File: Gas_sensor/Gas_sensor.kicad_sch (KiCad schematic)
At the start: 144 parts, among them J1 Conn_02x02_Counter_Clockwise, J2 Conn_01x04, J3 Conn_01x10, J4 Conn_01x01, J5 Conn_01x01, Q1 DMC1229UFDB, Q2 DMC1229UFDB, Q3 Q_NMOS_GSD, Q4 Q_NMOS_GSD, Q5 Q_NMOS_GSD, Q6 Q_NMOS_GSD, SW1 SW_Push, SW10 SW_Push, SW11 SW_Push, SW12 SW_Push, SW2 SW_Push, SW3 SW_Push, SW4 SW_Push, SW5 SW_Push, SW6 SW_Push, SW7 SW_Push, SW8 SW_Push, SW9 SW_Push, U1 LPV511, U10 MCP1700-3302E_SOT23, U11 STM32F401CCUx, U12 TMP117, U13 TPS63070, U14 TPS79333-EP, U15 REG102GA, U2 LPV511, U3 MCP47CMB22, U4 MCP6V71, U5 LPV511, U6 MCP6V71, U7 MCP6V71, U8 MCP6V71, U9 ADS1115IDGS, Y1 25MHz

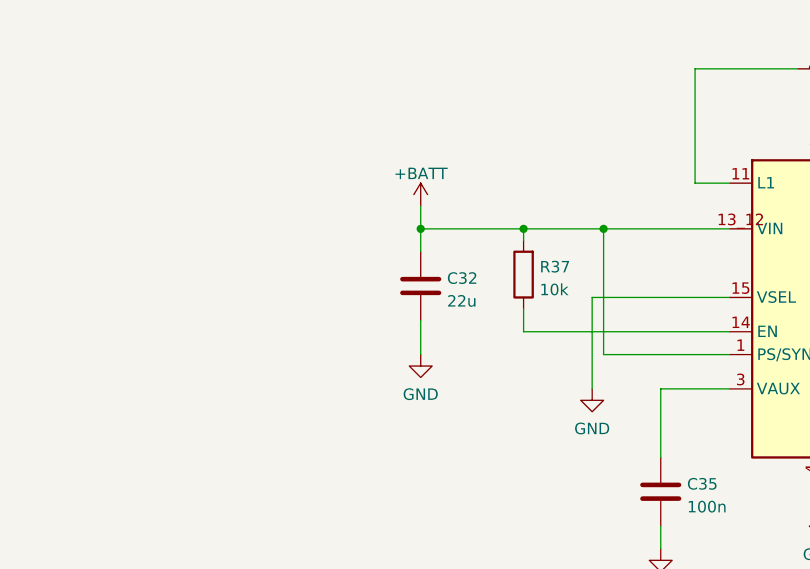
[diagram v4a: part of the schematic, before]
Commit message: gas sensor : place components
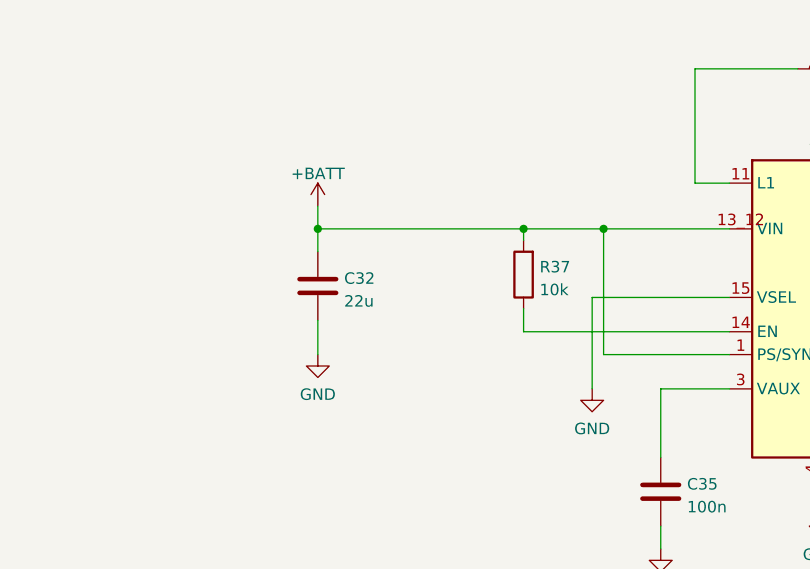
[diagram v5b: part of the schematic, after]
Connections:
- net at U3.5 (Vout1): now also R7.1
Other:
- moved on the sheet: C32
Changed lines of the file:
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@@
   (junction (at 237.49 318.77) (diameter 0) (color 0 0 0 0)
   )
-  (junction (at 466.09 82.55) (diameter 0) (color 0 0 0 0)
+  (junction (at 454.66 82.55) (diameter 0) (color 0 0 0 0)
   )
   (junction (at 497.84 279.4) (diameter 0) (color 0 0 0 0)
@@
     (stroke (width 0) (type default) (color 0 0 0 0))
   )
-  (wire (pts (xy 466.09 82.55) (xy 466.09 85.09))
+  (wire (pts (xy 454.66 82.55) (xy 454.66 85.09))
     (stroke (width 0) (type default) (color 0 0 0 0))
   )
@@
     (stroke (width 0) (type default) (color 0 0 0 0))
   )
-  (wire (pts (xy 477.52 82.55) (xy 466.09 82.55))
+  (wire (pts (xy 477.52 82.55) (xy 454.66 82.55))
     (stroke (width 0) (type default) (color 0 0 0 0))
   )
@@
     (stroke (width 0) (type default) (color 0 0 0 0))
   )
-  (wire (pts (xy 466.09 80.01) (xy 466.09 82.55))
+  (wire (pts (xy 454.66 80.01) (xy 454.66 82.55))
     (stroke (width 0) (type default) (color 0 0 0 0))
   )
@@
     (stroke (width 0) (type default) (color 0 0 0 0))
   )
-  (wire (pts (xy 466.09 92.71) (xy 466.09 96.52))
+  (wire (pts (xy 454.66 92.71) (xy 454.66 96.52))
     (stroke (width 0) (type default) (color 0 0 0 0))
   )
@@
     (pin "1")
   )
-  (symbol (lib_id "Device:C") (at 466.09 88.9 0) (unit 1)
+  (symbol (lib_id "Device:C") (at 454.66 88.9 0) (unit 1)
     (in_bom yes) (on_board yes) (fields_autoplaced)
-    (property "Reference" "C32" (id 0) (at 469.011 88.0653 0)
+    (property "Reference" "C32" (id 0) (at 457.581 88.0653 0)
       (effects (font (size 1.27 1.27)) (justify left))
     )
-    (property "Value" "22u" (id 1) (at 469.011 90.6022 0)
+    (property "Value" "22u" (id 1) (at 457.581 90.6022 0)
       (effects (font (size 1.27 1.27)) (justify left))
     )
-    (property "Footprint" "Yame_library:SM0603-MR" (id 2) (at 467.0552 92.71 0)
+    (property "Footprint" "Yame_library:SM0603-MR" (id 2) (at 455.6252 92.71 0)
       (effects (font (size 1.27 1.27)) hide)
     )
-    (property "Datasheet" "~" (id 3) (at 466.09 88.9 0)
+    (property "Datasheet" "~" (id 3) (at 454.66 88.9 0)
       (effects (font (size 1.27 1.27)) hide)
     )
@@
     (pin "2")
   )
-  (symbol (lib_id "power:+BATT") (at 466.09 80.01 0) (unit 1)
+  (symbol (lib_id "power:+BATT") (at 454.66 80.01 0) (unit 1)
     (in_bom yes) (on_board yes) (fields_autoplaced)
-    (property "Reference" "#PWR0104" (id 0) (at 466.09 83.82 0)
+    (property "Reference" "#PWR0104" (id 0) (at 454.66 83.82 0)
       (effects (font (size 1.27 1.27)) hide)
     )
-    (property "Value" "+BATT" (id 1) (at 466.09 76.4342 0))
-    (property "Footprint" "" (id 2) (at 466.09 80.01 0)
+    (property "Value" "+BATT" (id 1) (at 454.66 76.4342 0))
+    (property "Footprint" "" (id 2) (at 454.66 80.01 0)
       (effects (font (size 1.27 1.27)) hide)
     )
-    (property "Datasheet" "" (id 3) (at 466.09 80.01 0)
+    (property "Datasheet" "" (id 3) (at 454.66 80.01 0)
       (effects (font (size 1.27 1.27)) hide)
     )
@@
     (pin "2")
   )
-  (symbol (lib_id "power:GND") (at 466.09 96.52 0) (unit 1)
+  (symbol (lib_id "power:GND") (at 454.66 96.52 0) (unit 1)
     (in_bom yes) (on_board yes) (fields_autoplaced)
-    (property "Reference" "#PWR0105" (id 0) (at 466.09 102.87 0)
+    (property "Reference" "#PWR0105" (id 0) (at 454.66 102.87 0)
       (effects (font (size 1.27 1.27)) hide)
     )
-    (property "Value" "GND" (id 1) (at 466.09 100.9634 0))
-    (property "Footprint" "" (id 2) (at 466.09 96.52 0)
+    (property "Value" "GND" (id 1) (at 454.66 100.9634 0))
+    (property "Footprint" "" (id 2) (at 454.66 96.52 0)
       (effects (font (size 1.27 1.27)) hide)
     )
-    (property "Datasheet" "" (id 3) (at 466.09 96.52 0)
+    (property "Datasheet" "" (id 3) (at 454.66 96.52 0)
       (effects (font (size 1.27 1.27)) hide)
     )

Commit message: update layout
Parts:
- removed C27: 100n, Yame_library:SM0201-MR, symbol Device:C
- removed D1: BAT54C, Package_TO_SOT_SMD:SOT-23, symbol Diode:BAT54C
- added C46: 10u, Yame_library:SM0603-MR, symbol Device:C
- C16, C17, C18: footprint Yame_library:SM0603-MR -> Yame_library:SM0402-MR
- R1, R17, R19, R2, R24: footprint Yame_library:SM0402-MR -> Yame_library:SM0201-MR
- Y1: footprint Oscillator:Oscillator_SMD_Abracon_ASE-4Pin_3.2x2.5mm_HandSoldering -> Crystal:Crystal_SMD_3225-4Pin_3.2x2.5mm
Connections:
- net +3V3: now also C26.1, U11.1 (VBAT)
- net +BATT: now also C46.1
- net APO: now also U11.39 (PB3); no longer U11.46 (PB9)
- net GND: now also J1.2 (Pin_2), J1.3 (Pin_3), C46.2; no longer J1.1 (Pin_1), J1.4 (Pin_4)
- net ~{RDY}: now also U11.20 (PB2)
- net at U3.5 (Vout1): now also R7.1
- net at Q1.3 (D2), Q1.8 (D2), U7.3 (+): now also J1.1 (Pin_1); no longer J1.2 (Pin_2)
- net at Q2.3 (D2), Q2.8 (D2), U8.3 (+): now also J1.4 (Pin_4); no longer J1.3 (Pin_3)
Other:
- moved on the sheet: J1

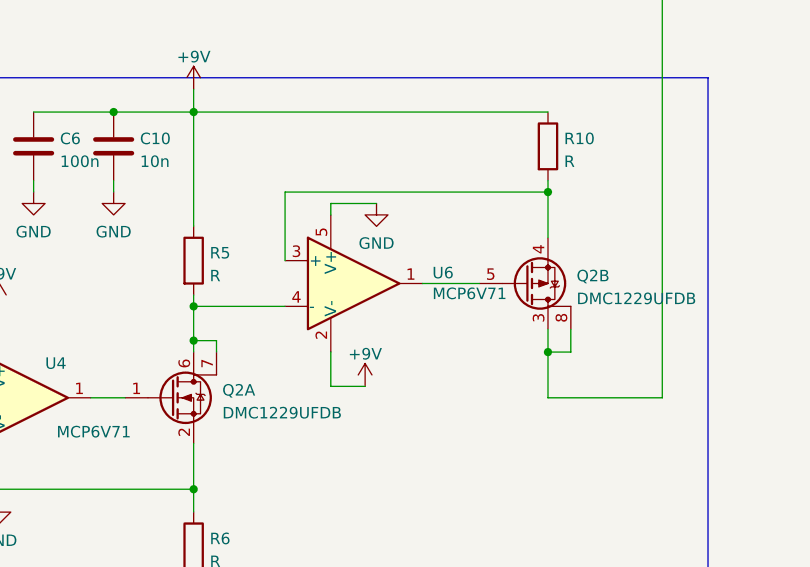
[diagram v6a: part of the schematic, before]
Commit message: Gas sensor : update layout
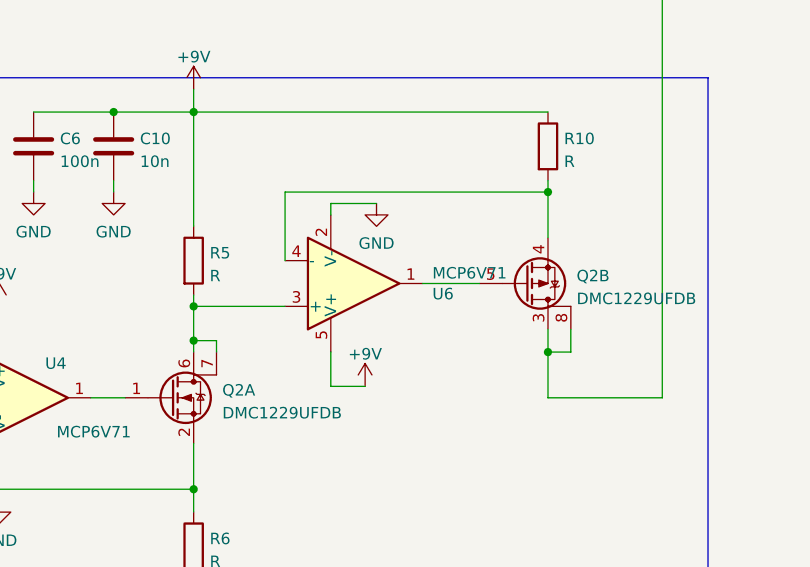
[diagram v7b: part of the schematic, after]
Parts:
- U1, U2: footprint Package_TO_SOT_SMD:SOT-23-5 -> Package_TO_SOT_SMD:SOT-353_SC-70-5
- U4: footprint Package_TO_SOT_SMD:SOT-353_SC-70-5 -> Package_TO_SOT_SMD:SOT-23-5
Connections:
- net +9V: now also U6.5 (V+); no longer U6.2 (V-)
- net GND: now also U6.2 (V-); no longer U6.5 (V+)
- net at Q2.4 (S2), R10.2: now also U6.4 (-); no longer U6.3 (+)
- net at Q2.6 (D1), Q2.7 (D1), R5.2: now also U6.3 (+); no longer U6.4 (-)
- net at U3.5 (Vout1): now also R7.1
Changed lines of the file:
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@@
       (effects (font (size 1.27 1.27)) (justify left))
     )
-    (property "Footprint" "Package_TO_SOT_SMD:SOT-23-5" (id 2) (at 110.49 87.63 0)
+    (property "Footprint" "Package_TO_SOT_SMD:SOT-353_SC-70-5" (id 2) (at 110.49 87.63 0)
       (effects (font (size 1.27 1.27)) (justify left) hide)
     )
@@
     (pin "2")
   )
-  (symbol (lib_id "Amplifier_Operational:LPV811DBV") (at 166.37 207.01 0) (unit 1)
+  (symbol (lib_id "Amplifier_Operational:LPV811DBV") (at 166.37 207.01 0) (mirror x) (unit 1)
     (in_bom yes) (on_board yes)
-    (property "Reference" "U6" (id 0) (at 175.1076 205.8416 0)
+    (property "Reference" "U6" (id 0) (at 175.1076 208.1784 0)
       (effects (font (size 1.27 1.27)) (justify left))
     )
-    (property "Value" "MCP6V71" (id 1) (at 175.1076 208.153 0)
+    (property "Value" "MCP6V71" (id 1) (at 175.1076 205.867 0)
       (effects (font (size 1.27 1.27)) (justify left))
     )
-    (property "Footprint" "Package_TO_SOT_SMD:SOT-23-5" (id 2) (at 163.83 212.09 0)
+    (property "Footprint" "Package_TO_SOT_SMD:SOT-23-5" (id 2) (at 163.83 201.93 0)
       (effects (font (size 1.27 1.27)) (justify left) hide)
     )
-    (property "Datasheet" "https://www.ti.com/lit/ds/symlink/lpv812.pdf" (id 3) (at 166.37 201.93 0)
+    (property "Datasheet" "https://www.ti.com/lit/ds/symlink/lpv812.pdf" (id 3) (at 166.37 212.09 0)
       (effects (font (size 1.27 1.27)) hide)
     )
@@
       (effects (font (size 1.27 1.27)) (justify left))
     )
-    (property "Footprint" "Package_TO_SOT_SMD:SOT-353_SC-70-5" (id 2) (at 127 224.79 0)
+    (property "Footprint" "Package_TO_SOT_SMD:SOT-23-5" (id 2) (at 127 224.79 0)
       (effects (font (size 1.27 1.27)) (justify left) hide)
     )
@@
       (effects (font (size 1.27 1.27)) (justify left))
     )
-    (property "Footprint" "Package_TO_SOT_SMD:SOT-23-5" (id 2) (at 68.58 354.33 0)
+    (property "Footprint" "Package_TO_SOT_SMD:SOT-353_SC-70-5" (id 2) (at 68.58 354.33 0)
       (effects (font (size 1.27 1.27)) (justify left) hide)
     )
@@
     )
     (path "/c639d856-1978-4de2-9271-4ecaf053f77d"
-      (reference "U1") (unit 1) (value "LPV511") (footprint "Package_TO_SOT_SMD:SOT-23-5")
+      (reference "U1") (unit 1) (value "LPV511") (footprint "Package_TO_SOT_SMD:SOT-353_SC-70-5")
     )
     (path "/00000000-0000-0000-0000-000062f6e0e7"
-      (reference "U2") (unit 1) (value "LPV511") (footprint "Package_TO_SOT_SMD:SOT-23-5")
+      (reference "U2") (unit 1) (value "LPV511") (footprint "Package_TO_SOT_SMD:SOT-353_SC-70-5")
     )
     (path "/3bc90c99-6b90-4d5e-a510-a209a2e89490"
@@
     )
     (path "/a6f7638d-f863-4fef-b4b7-b44c93155bb9"
-      (reference "U4") (unit 1) (value "MCP6V71") (footprint "Package_TO_SOT_SMD:SOT-353_SC-70-5")
+      (reference "U4") (unit 1) (value "MCP6V71") (footprint "Package_TO_SOT_SMD:SOT-23-5")
     )
     (path "/ea765fe7-c21d-4dd9-96b4-f61518ce7189"

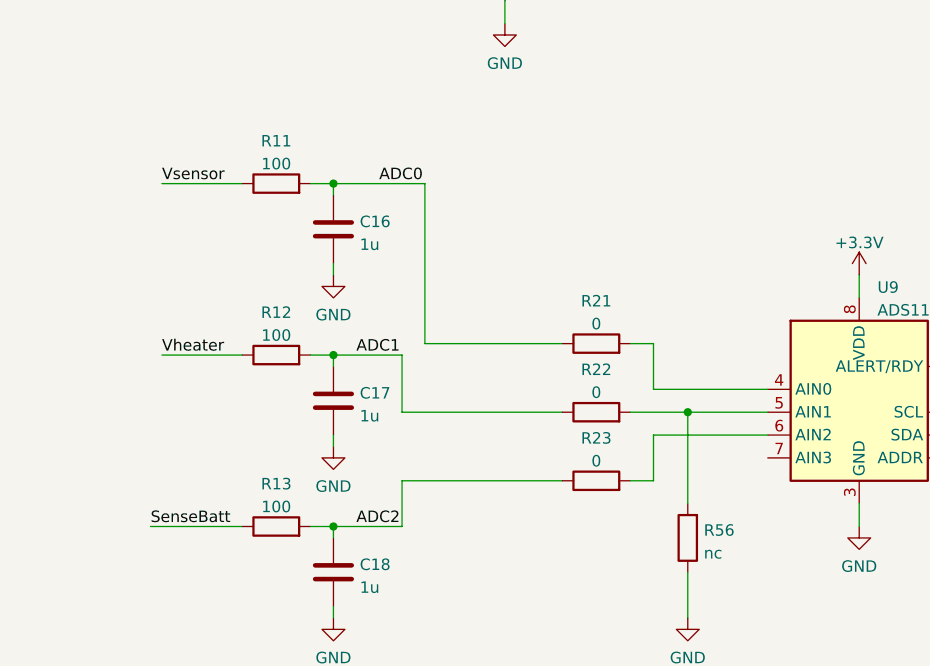
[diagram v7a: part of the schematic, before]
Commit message: gas sensor : update layout
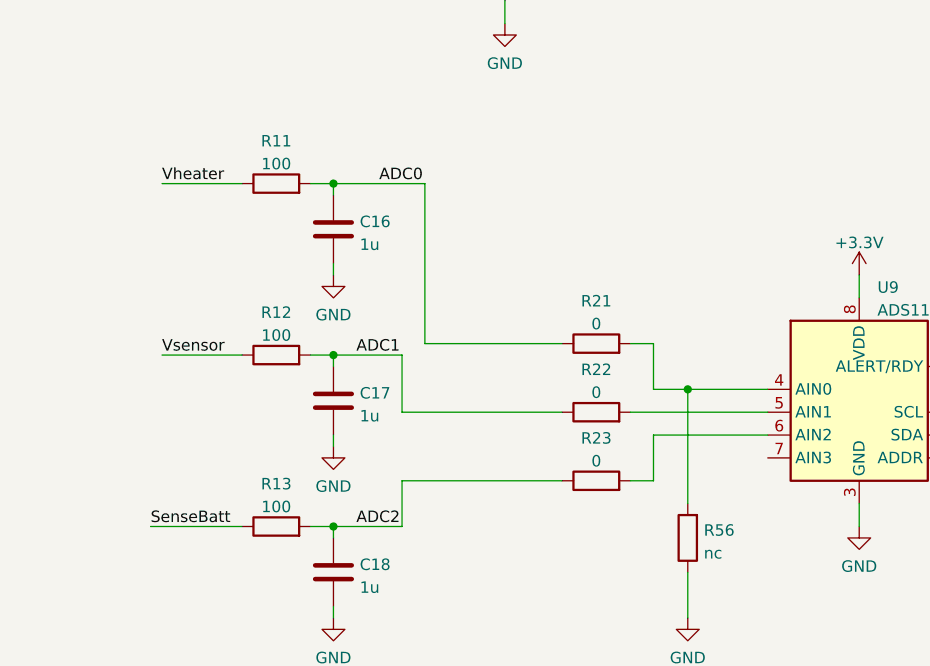
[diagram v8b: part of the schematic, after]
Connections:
- net Vheater: now also R11.1; no longer R12.1
- net Vsensor: now also R12.1; no longer R11.1
- net at R22.2, U9.5 (AIN1): no longer R56.2
- net at U3.5 (Vout1): now also R7.1
- net at R21.2, U9.4 (AIN0): now also R56.2
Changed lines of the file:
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@@
   (junction (at 237.49 356.87) (diameter 0) (color 0 0 0 0)
   )
+  (junction (at 276.86 341.63) (diameter 0) (color 0 0 0 0)
+  )
   (junction (at 312.42 114.3) (diameter 0) (color 0 0 0 0)
   )
@@
   (junction (at 438.15 152.4) (diameter 0) (color 0 0 0 0)
   )
-  (junction (at 276.86 344.17) (diameter 0) (color 0 0 0 0)
-  )
   (junction (at 132.08 76.2) (diameter 0) (color 0 0 0 0)
   )
@@
     (stroke (width 0) (type default) (color 0 0 0 0))
   )
-  (wire (pts (xy 273.05 341.63) (xy 285.75 341.63))
+  (wire (pts (xy 273.05 341.63) (xy 276.86 341.63))
     (stroke (width 0) (type default) (color 0 0 0 0))
   )
@@
     (stroke (width 0) (type default) (color 0 0 0 0))
   )
+  (wire (pts (xy 276.86 341.63) (xy 285.75 341.63))
+    (stroke (width 0) (type default) (color 0 0 0 0))
+  )
   (wire (pts (xy 542.29 106.68) (xy 542.29 105.41))
     (stroke (width 0) (type default) (color 0 0 0 0))
@@
     (stroke (width 0) (type default) (color 0 0 0 0))
   )
+  (wire (pts (xy 276.86 341.63) (xy 276.86 354.33))
+    (stroke (width 0) (type default) (color 0 0 0 0))
+  )
   (wire (pts (xy 306.07 346.71) (xy 311.15 346.71))
     (stroke (width 0) (type default) (color 0 0 0 0))
@@
     (stroke (width 0) (type default) (color 0 0 0 0))
   )
-  (wire (pts (xy 276.86 344.17) (xy 285.75 344.17))
-    (stroke (width 0) (type default) (color 0 0 0 0))
-  )
   (wire (pts (xy 387.35 212.09) (xy 393.7 212.09))
     (stroke (width 0) (type default) (color 0 0 0 0))
@@
     (stroke (width 0) (type default) (color 0 0 0 0))
   )
-  (wire (pts (xy 270.51 344.17) (xy 276.86 344.17))
+  (wire (pts (xy 270.51 344.17) (xy 285.75 344.17))
     (stroke (width 0) (type default) (color 0 0 0 0))
   )
@@
     (stroke (width 0) (type default) (color 0 0 0 0))
   )
-  (wire (pts (xy 276.86 344.17) (xy 276.86 354.33))
-    (stroke (width 0) (type default) (color 0 0 0 0))
-  )
   (wire (pts (xy 477.52 82.55) (xy 477.52 83.82))
     (stroke (width 0) (type default) (color 0 0 0 0))
@@
     (effects (font (size 1.27 1.27)) (justify left bottom))
   )
-  (label "Vsensor" (at 218.44 318.77 0)
-    (effects (font (size 1.27 1.27)) (justify left bottom))
-  )
   (label "Buzzer_EN" (at 265.43 293.37 0)
     (effects (font (size 1.27 1.27)) (justify left bottom))
@@
     (effects (font (size 1.27 1.27)) (justify left bottom))
   )
+  (label "Vheater" (at 218.44 318.77 0)
+    (effects (font (size 1.27 1.27)) (justify left bottom))
+  )
+  (label "Vsensor" (at 218.44 337.82 0)
+    (effects (font (size 1.27 1.27)) (justify left bottom))
+  )
   (label "Vheater" (at 241.3 187.96 0)
     (effects (font (size 1.27 1.27)) (justify left bottom))
@@
     (effects (font (size 1.27 1.27)) (justify left bottom))
   )
-  (label "Vheater" (at 218.44 337.82 0)
-    (effects (font (size 1.27 1.27)) (justify left bottom))
-  )
